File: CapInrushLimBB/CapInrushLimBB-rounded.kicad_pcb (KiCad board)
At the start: 2 copper layers, 56.5 x 34.9 mm, 29 parts, among them J1 Screw_Terminal_01x02, J2 Screw_Terminal_01x02, K1 G5LE-1A, Q1 MPSA42, Q2 IRF9540N, Q3 MPSA42, Q4 Q_PMOS_GDSD

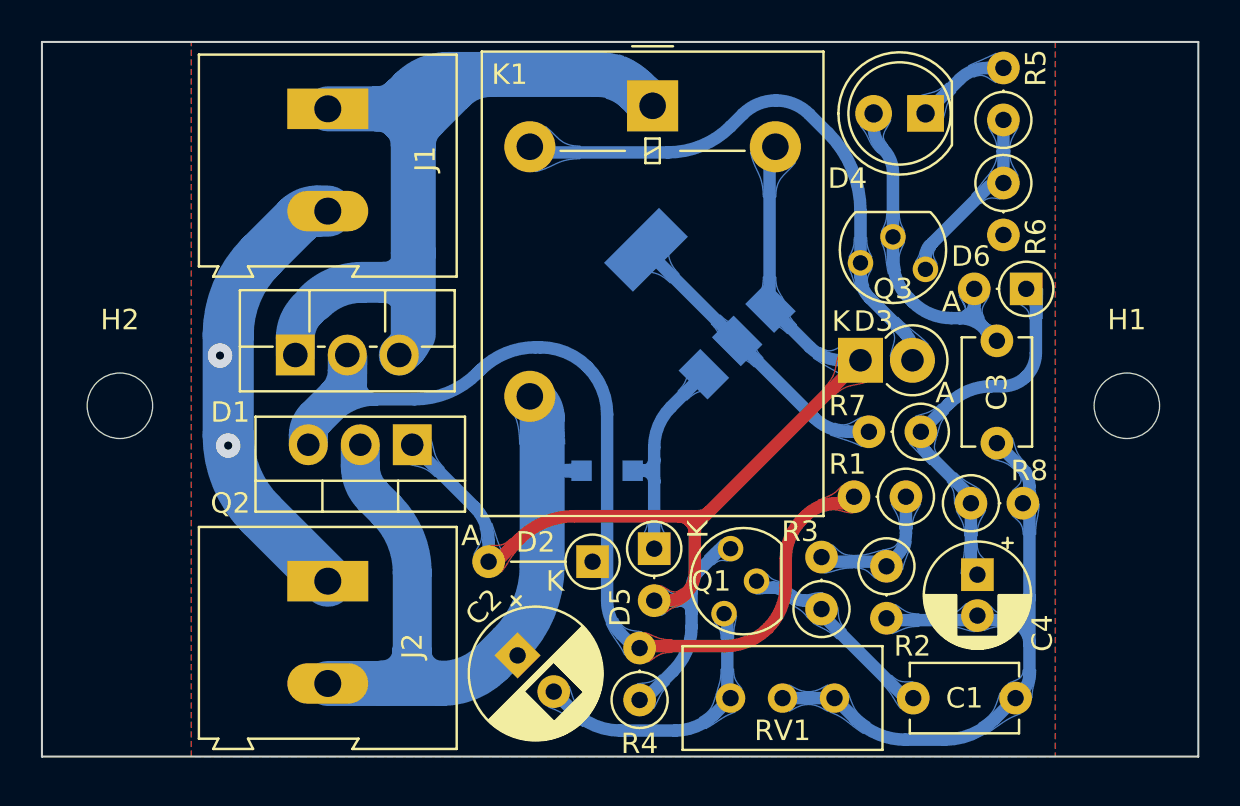
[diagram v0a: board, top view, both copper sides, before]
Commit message: Updated rounded tracks version of updates for low voltage use.
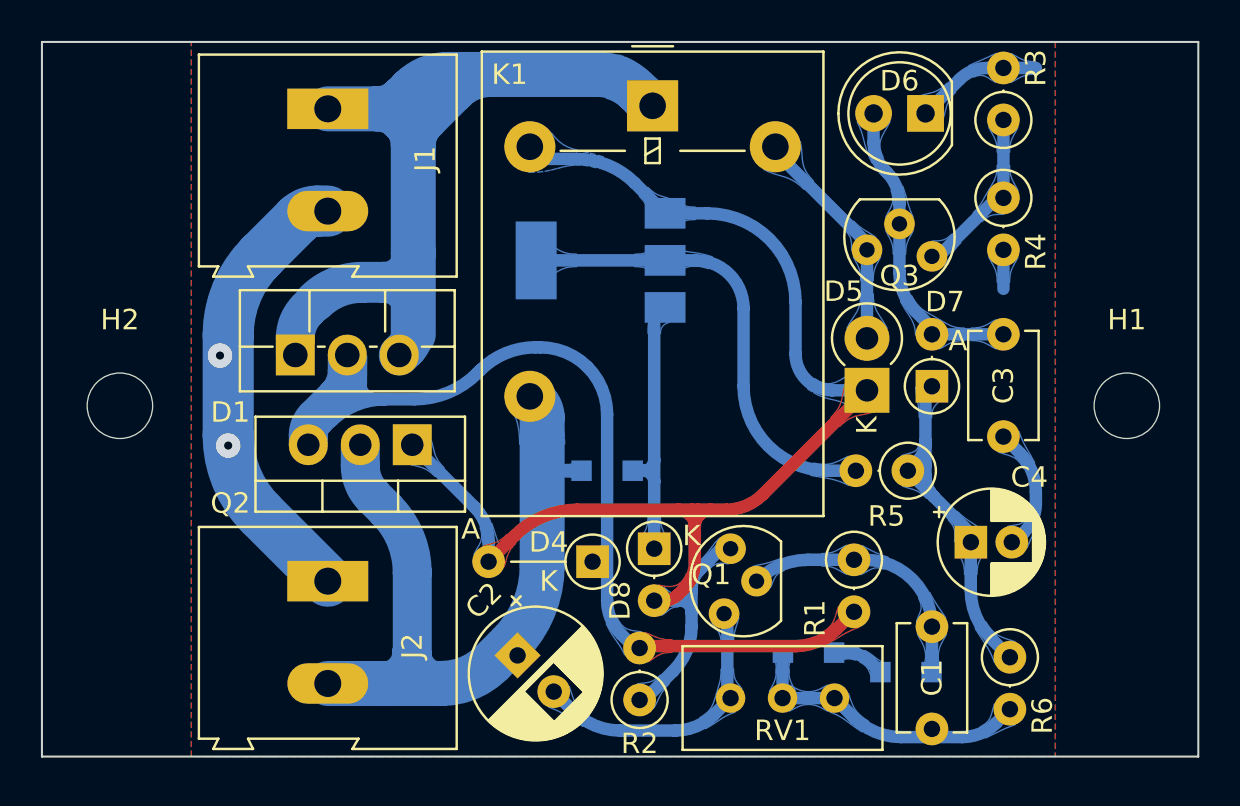
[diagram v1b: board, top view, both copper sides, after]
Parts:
- removed the R2 at (248.3, 151.0)
- removed the R3 at (245.1, 153.1)
- added D2: BAS16H, Diode_SMD:D_SOD-323_HandSoldering, B.Cu at (249.2, 156.2)
- added D3: BAS16H, Diode_SMD:D_SOD-323_HandSoldering, B.Cu at (244.5, 155.3)
- C1: value 220nF 50V -> 680nF 100V
- Q4: value Q_PMOS_GDSD -> BSP230 300V 0.21A
- moved R6 7.76 mm to (254.3, 155.5), turned to -90 degrees
- moved D7 6.63 mm to (250.5, 142.2), turned to 90 degrees
- moved Q4 4.76 mm to (234.3, 136.1), turned to 180 degrees
- moved R1 3.99 mm to (246.7, 150.7), turned to -90 degrees
- moved C1 3.61 mm to (250.5, 154.0), turned to -90 degrees
- moved R5 2.01 mm to (249.3, 146.4)
- moved C4 1.62 mm to (252.4, 149.9), turned to 0 degrees
- moved D5 1.50 mm to (247.3, 142.4), turned to 90 degrees
- moved R4 0.73 mm to (254.0, 133.0)
- moved Q3 0.71 mm to (250.2, 134.9)
- moved C3 0.45 mm to (254.0, 144.7)
- renumbered D2 to D4, D3 to D5, D4 to D6, D6 to D7, D5 to D8, D7 to D9, R4 to R2, R5 to R3, R6 to R4, R7 to R5, R8 to R6
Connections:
- K1 pad 2: /RLCoilLow -> /RLCoilHigh
- K1 pad 4: /RLCoilHigh -> /RLCoilLow
- R1 pad 1: Net-(R1-Pad1) -> Net-(C1-Pad1)
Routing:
- net /RLCoilLow: track 28.4 -> 11.2 mm
- net /Gnd: track 61.9 -> 50.9 mm
- net /RLCoilHigh: track 63.4 -> 72.7 mm
- net Net-(Q4-Pad2): track 14.5 -> 22.9 mm
- net Net-(R1-Pad1): track 6.97 -> 0.00 mm
- net /PolProtect: track 55.1 -> 49.2 mm
- net Net-(C1-Pad1): track 9.50 -> 12.8 mm
- net Net-(C3-Pad2): track 17.6 -> 14.4 mm
- net Net-(D2-Pad1): track 0.00 -> 2.58 mm
- net Net-(D8-Pad1): track 11.6 -> 14.0 mm
- net Net-(Q3-Pad1): track 8.98 -> 8.37 mm
